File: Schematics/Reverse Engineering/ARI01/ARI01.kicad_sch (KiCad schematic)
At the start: 159 parts, among them J1 Conn_01x40, Q1 PNP, Q10 PNP, Q11 PNP, Q12 PNP, Q13 PNP, Q14 PNP, Q15 PNP, Q16 PNP, Q17 PNP, Q18 PNP, Q19 PNP, Q2 PNP, Q20 PNP, Q21 PNP, Q22 PNP, Q23 PNP, Q24 PNP, Q3 PNP, Q4 PNP, Q5 PNP, Q6 PNP, Q7 PNP, Q8 PNP, Q9 PNP

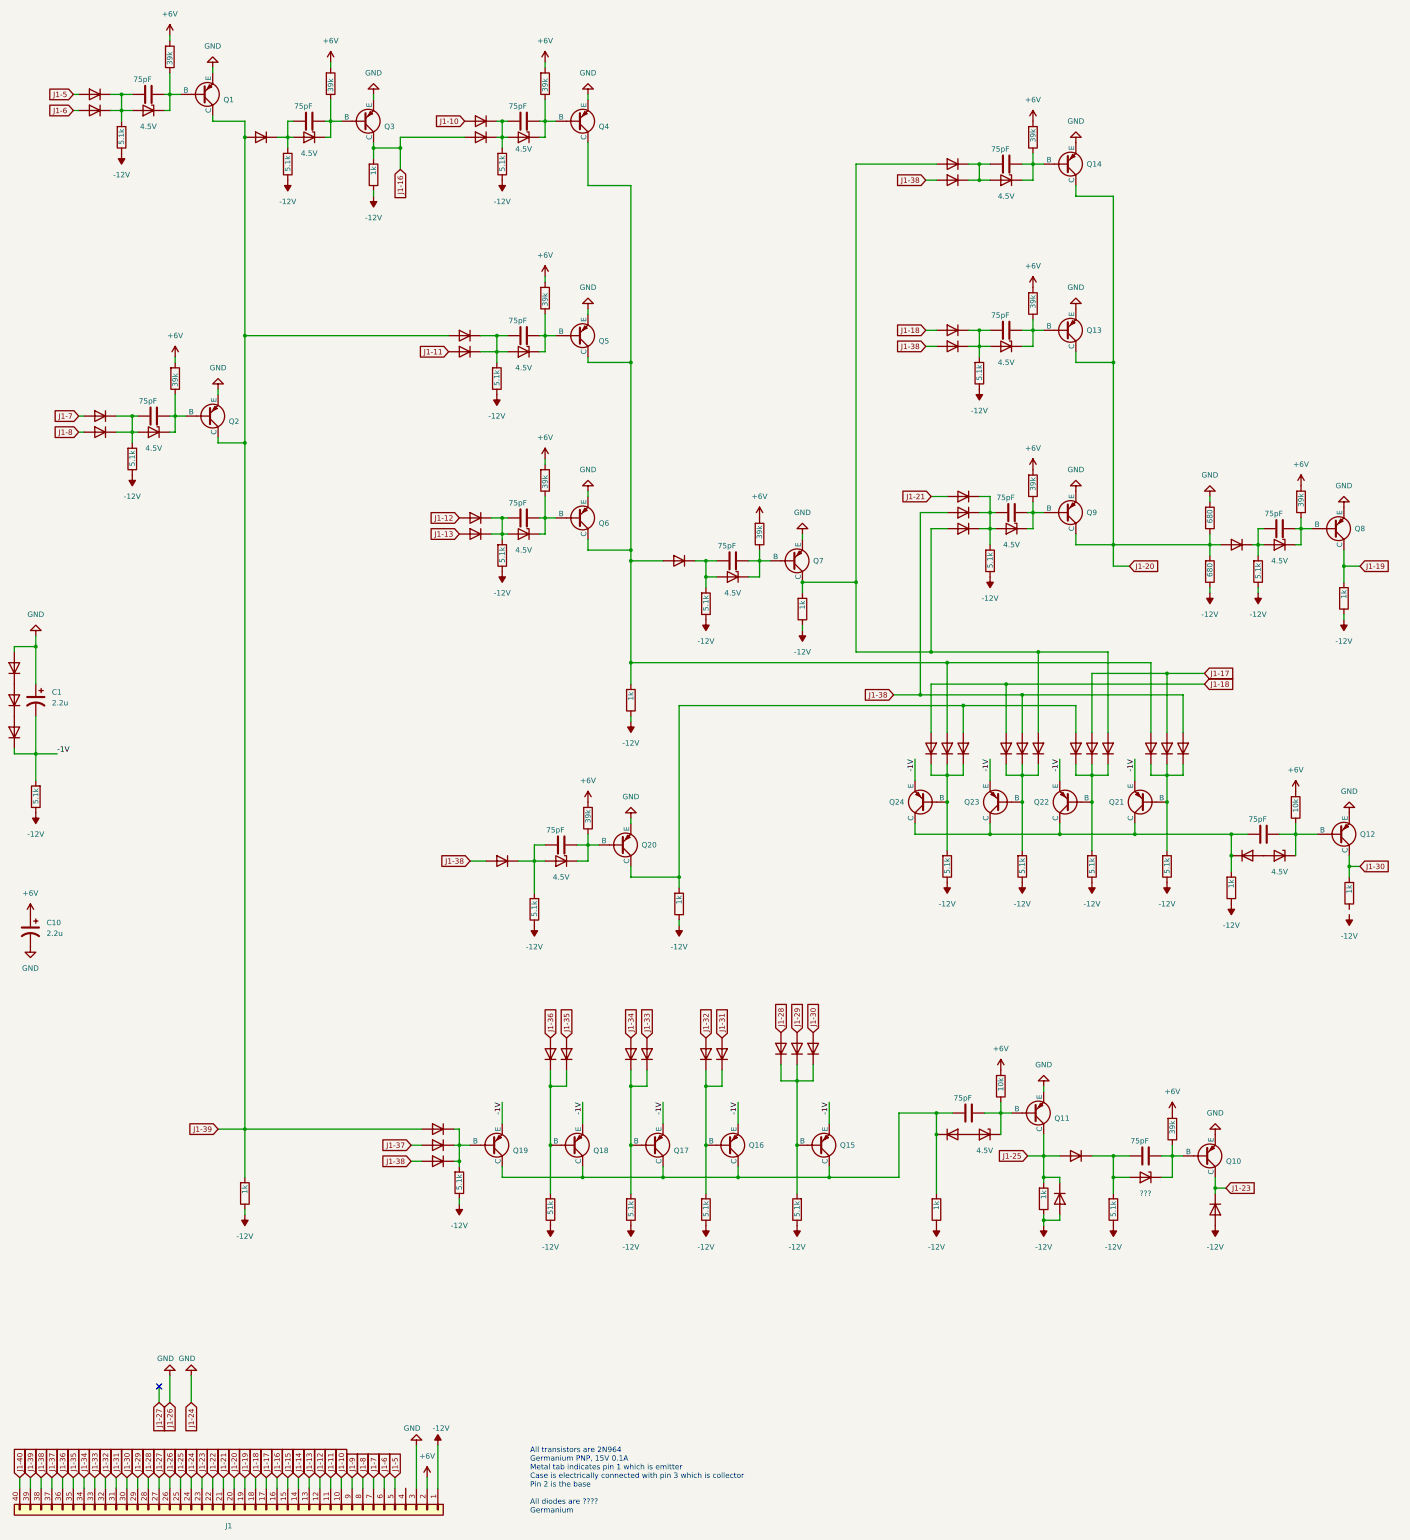
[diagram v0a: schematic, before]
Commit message: Fixed an error in carry logic of ARI01, and drew up a logisim functional model
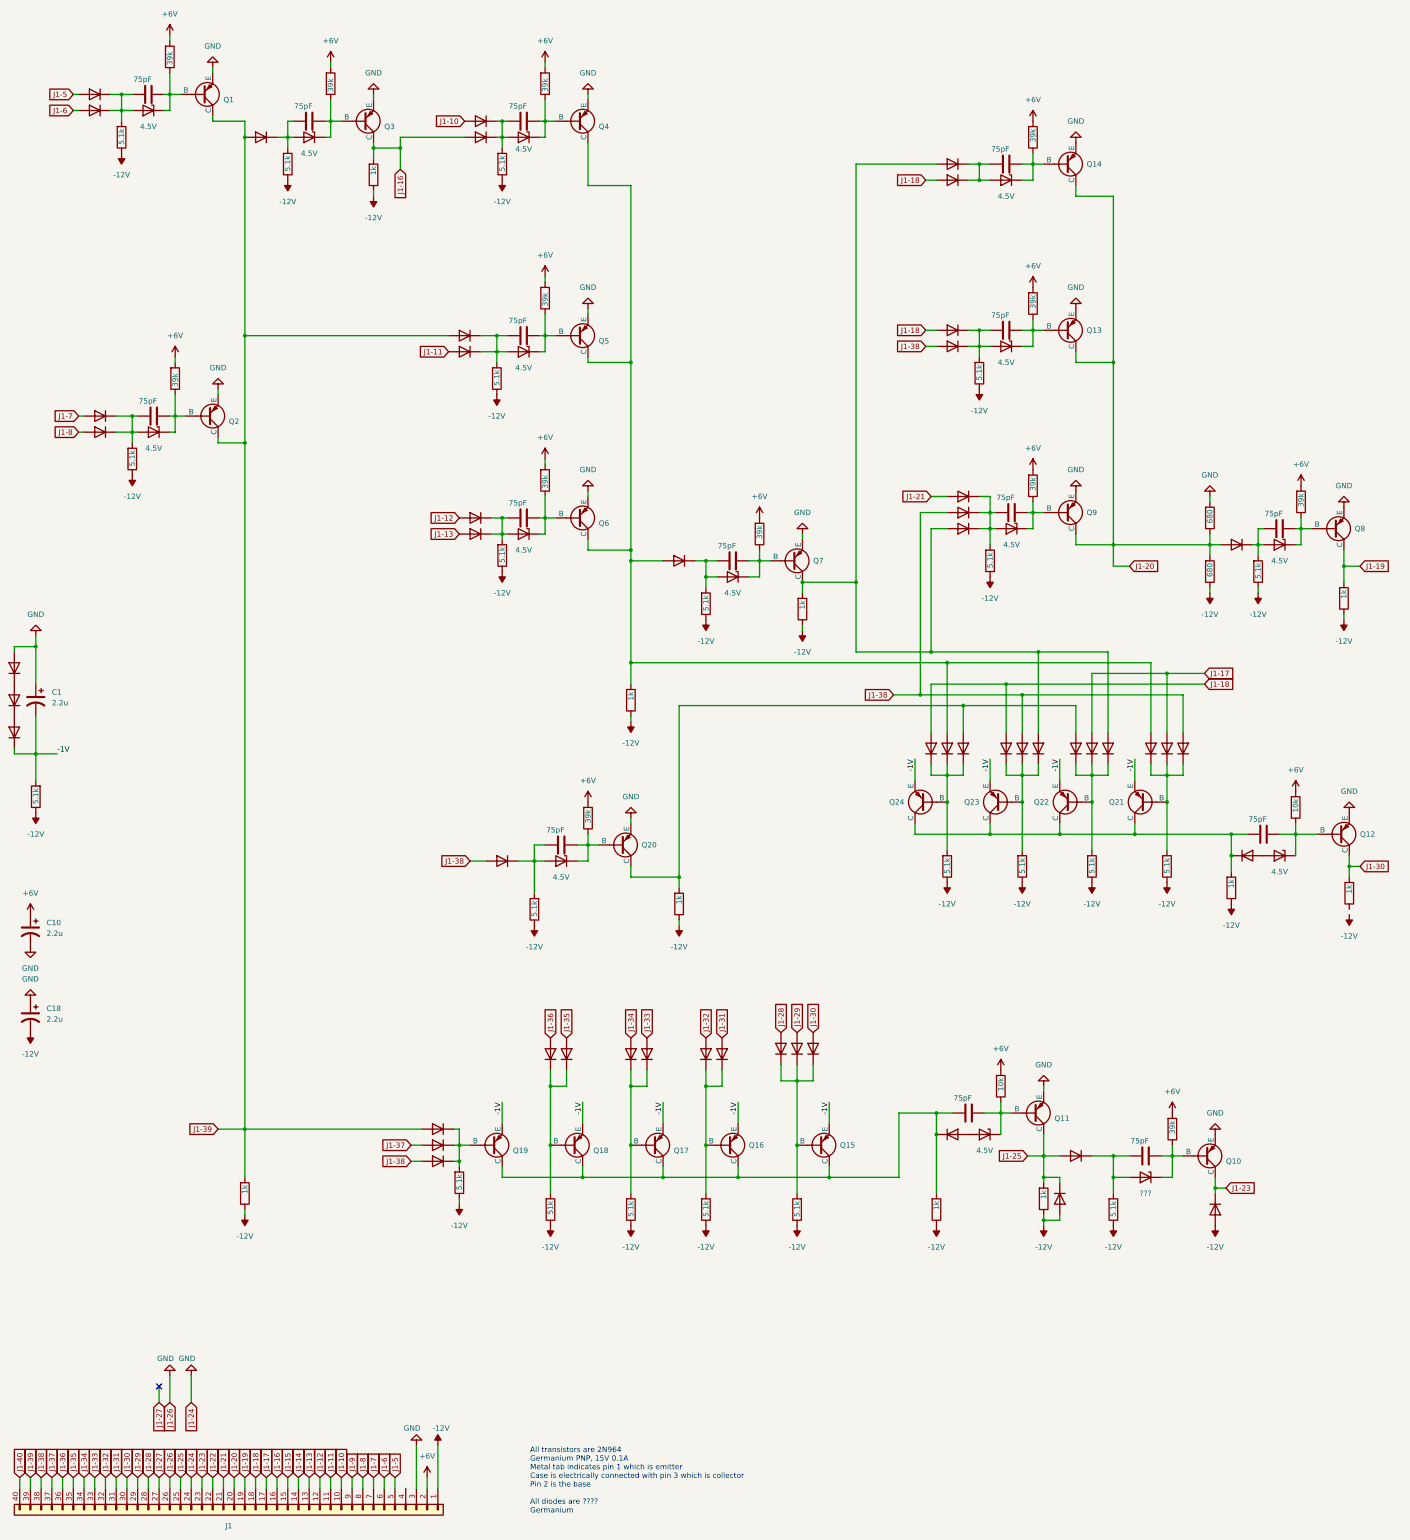
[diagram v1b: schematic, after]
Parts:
- added C18: 2.2u, symbol Device:C_Polarized_US
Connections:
- net -12V: now also C18.2
- net GND: now also C18.1
- net J1-18: now also D67.2 (A)
- net J1-38: no longer D67.2 (A)
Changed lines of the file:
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@@
 	(global_label "J1-18"
 		(shape input)
+		(at 243.84 78.74 180)
+		(fields_autoplaced yes)
+		(effects
+			(font
+				(size 1.27 1.27)
+			)
+			(justify right)
+		)
+		(property "Intersheetrefs" "${INTERSHEET_REFS}"
+			(at 234.6863 78.74 0)
+			(effects
+				(font
+					(size 1.27 1.27)
+				)
+				(justify right)
+				(hide yes)
+			)
+		)
+	)
+	(global_label "J1-18"
+		(shape input)
 		(at 309.88 198.12 0)
 		(fields_autoplaced yes)
@@
 		)
 	)
-	(global_label "J1-38"
-		(shape input)
-		(at 243.84 78.74 180)
-		(fields_autoplaced yes)
-		(effects
-			(font
-				(size 1.27 1.27)
-			)
-			(justify right)
-		)
-		(property "Intersheetrefs" "${INTERSHEET_REFS}"
-			(at 234.6863 78.74 0)
-			(effects
-				(font
-					(size 1.27 1.27)
-				)
-				(justify right)
-				(hide yes)
-			)
-		)
-	)
 	(global_label "J1-31"
 		(shape input)
@@
 	)
 	(symbol
+		(lib_id "power:-12V")
+		(at 31.75 280.67 0)
+		(mirror x)
+		(unit 1)
+		(exclude_from_sim no)
+		(in_bom yes)
+		(on_board yes)
+		(dnp no)
+		(fields_autoplaced yes)
+		(property "Reference" "#PWR075"
+			(at 31.75 276.86 0)
+			(effects
+				(font
+					(size 1.27 1.27)
+				)
+				(hide yes)
+			)
+		)
+		(property "Value" "-12V"
+			(at 31.75 285.75 0)
+			(effects
+				(font
+					(size 1.27 1.27)
+				)
+			)
+		)
+		(property "Footprint" ""
+			(at 31.75 280.67 0)
+			(effects
+				(font
+					(size 1.27 1.27)
+				)
+				(hide yes)
+			)
+		)
+		(property "Datasheet" ""
+			(at 31.75 280.67 0)
+			(effects
+				(font
+					(size 1.27 1.27)
+				)
+				(hide yes)
+			)
+		)
+		(property "Description" "Power symbol creates a global label with name \"-12V\""
+			(at 31.75 280.67 0)
+			(effects
+				(font
+					(size 1.27 1.27)
+				)
+				(hide yes)
+			)
+		)
+		(pin "1"
+		)
+		(instances
+			(project "ARI01"
+				(path "/f51c7135-0e36-43b2-ae27-ed556c89e1ef"
+					(reference "#PWR075")
+					(unit 1)
+				)
+			)
+		)
+	)
+	(symbol
 		(lib_id "Device:R")
 		(at 154.94 322.58 0)
@@
 	)
 	(symbol
+		(lib_id "Device:C_Polarized_US")
+		(at 31.75 276.86 0)
+		(mirror y)
+		(unit 1)
+		(exclude_from_sim no)
+		(in_bom yes)
+		(on_board yes)
+		(dnp no)
+		(fields_autoplaced yes)
+		(property "Reference" "C18"
+			(at 35.56 274.9549 0)
+			(effects
+				(font
+					(size 1.27 1.27)
+				)
+				(justify right)
+			)
+		)
+		(property "Value" "2.2u"
+			(at 35.56 277.4949 0)
+			(effects
+				(font
+					(size 1.27 1.27)
+				)
+				(justify right)
+			)
+		)
+		(property "Footprint" ""
+			(at 31.75 276.86 0)
+			(effects
+				(font
+					(size 1.27 1.27)
+				)
+				(hide yes)
+			)
+		)
+		(property "Datasheet" "~"
+			(at 31.75 276.86 0)
+			(effects
+				(font
+					(size 1.27 1.27)
+				)
+				(hide yes)
+			)
+		)
+		(property "Description" "Polarized capacitor, US symbol"
+			(at 31.75 276.86 0)
+			(effects
+				(font
+					(size 1.27 1.27)
+				)
+				(hide yes)
+			)
+		)
+		(pin "2"
+		)
+		(pin "1"
+		)
+		(instances
+			(project "ARI01"
+				(path "/f51c7135-0e36-43b2-ae27-ed556c89e1ef"
+					(reference "C18")
+					(unit 1)
+				)
+			)
+		)
+	)
+	(symbol
 		(lib_id "Simulation_SPICE:PNP")
 		(at 295.91 226.06 180)
@@
 					(unit 1)
 				)
+			)
+		)
+	)
+	(symbol
+		(lib_id "power:GND")
+		(at 31.75 273.05 180)
+		(unit 1)
+		(exclude_from_sim no)
+		(in_bom yes)
+		(on_board yes)
+		(dnp no)
+		(fields_autoplaced yes)
+		(property "Reference" "#PWR074"
+			(at 31.75 266.7 0)
+			(effects
+				(font
+					(size 1.27 1.27)
+				)
+				(hide yes)
+			)
+		)
+		(property "Value" "GND"
+			(at 31.75 267.97 0)
+			(effects
+				(font
+					(size 1.27 1.27)
+				)
+			)
+		)
+		(property "Footprint" ""
+			(at 31.75 273.05 0)
+			(effects
+				(font
+					(size 1.27 1.27)
+				)
+				(hide yes)
+			)
+		)
+		(property "Datasheet" ""
+			(at 31.75 273.05 0)
+			(effects
+				(font
+					(size 1.27 1.27)
+				)
+				(hide yes)
+			)
+		)
+		(property "Description" "Power symbol creates a global label with name \"GND\" , ground"
+			(at 31.75 273.05 0)
+			(effects
+				(font
+					(size 1.27 1.27)
+				)
+				(hide yes)
+			)
+		)
+		(pin "1"
+		)
+		(instances
+			(project "ARI01"
+				(path "/f51c7135-0e36-43b2-ae27-ed556c89e1ef"
+					(reference "#PWR074")
+					(unit 1)
+				)
